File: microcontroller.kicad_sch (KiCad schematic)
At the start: 19 parts, among them J7 Conn_02x10_Odd_Even, J8 Conn_ST_STDC14, Q8 NPN, SW1 SW_Push, U10 MCP9808T-E/MS, U2 STM32G491KEU6

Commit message: PCB 2025 rev2
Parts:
- added R29, R30: 2k2, Resistor_SMD:R_0805_2012Metric_Pad1.20x1.40mm_HandSolder, symbol Device:R
- added TP10, TP9: TestPoint, TestPoint:TestPoint_Bridge_Pitch2.0mm_Drill0.7mm, symbol Connector:TestPoint
- C11: value 4.7u -> 4u7
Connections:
- net 3V3: now also R29.2, R30.1
- net SCL: now also R29.1, TP9.1
- net SDA: now also R30.2, TP10.1

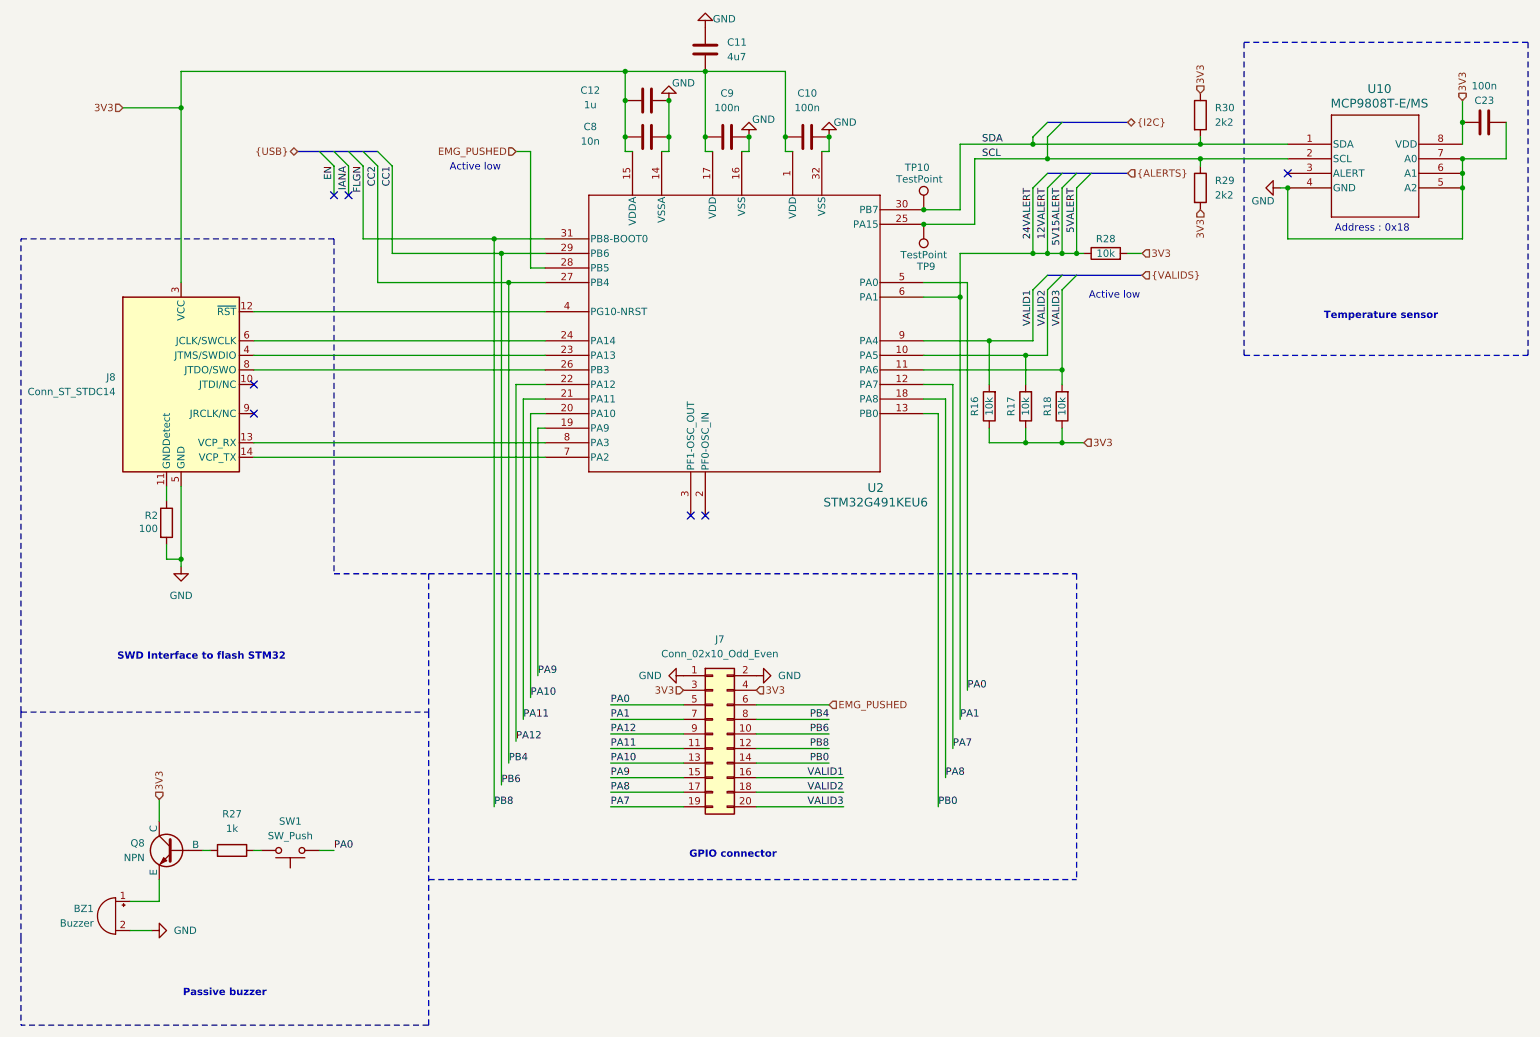
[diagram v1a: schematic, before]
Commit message: nouvelle version : correction erreurs, ameliorations qualite, passage a 4 couches, ajout pilotage des traco depuis le stm32
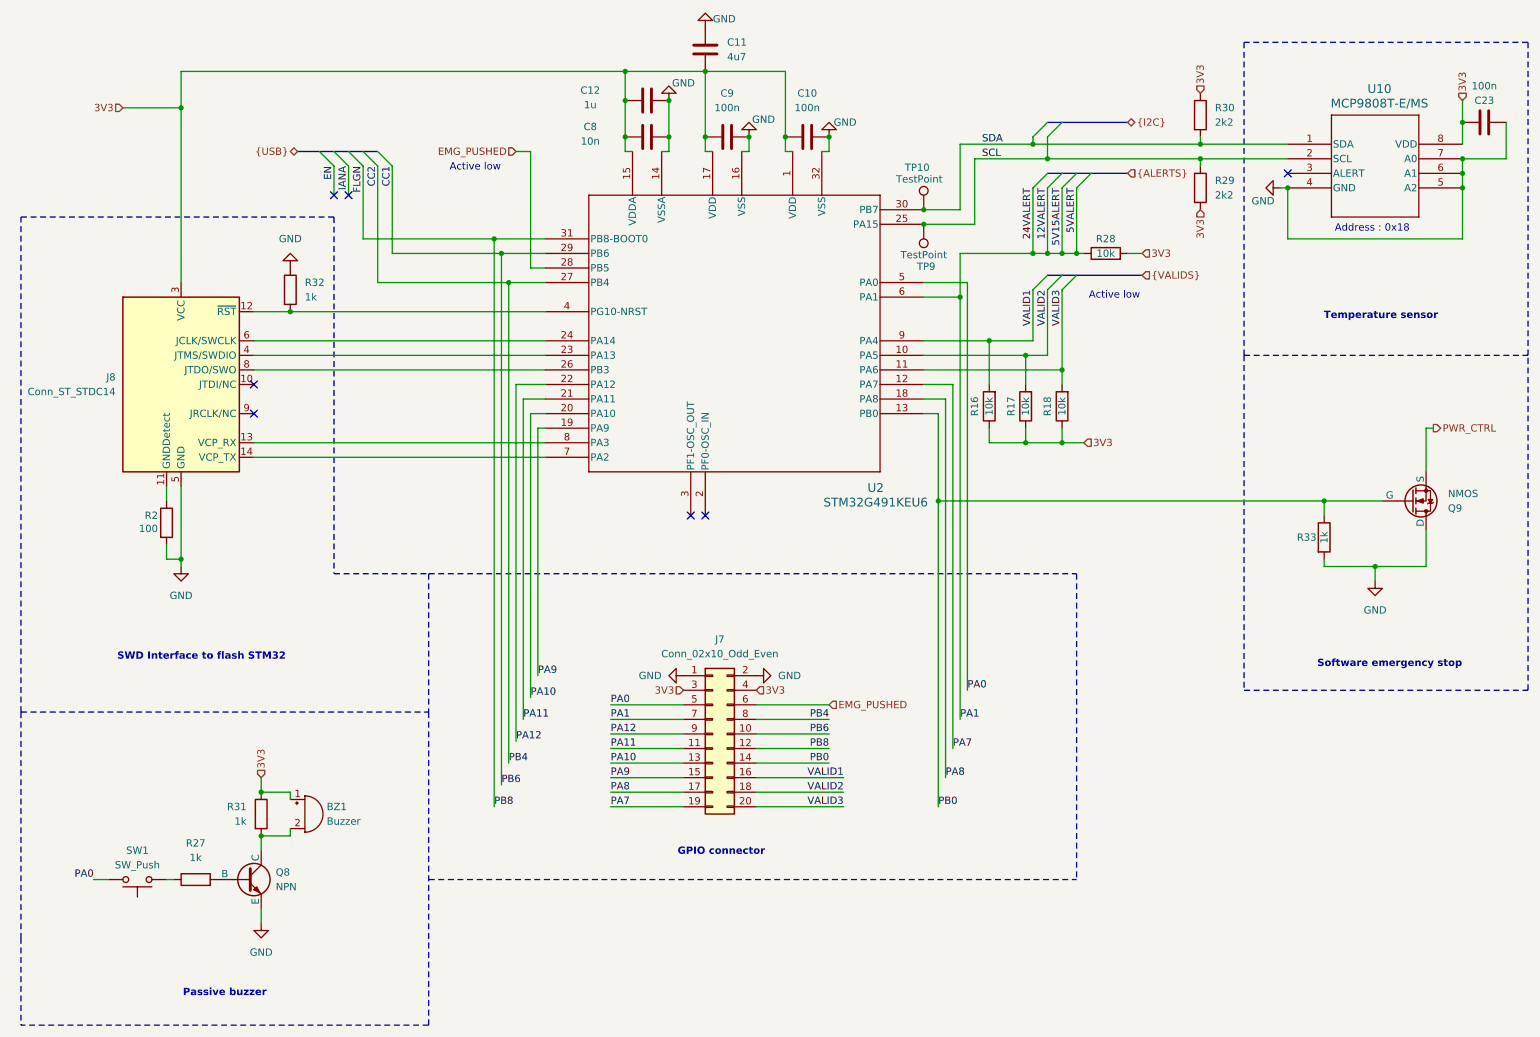
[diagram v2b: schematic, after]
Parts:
- added Q9: NMOS, Package_TO_SOT_SMD:SOT-23, symbol Simulation_SPICE:NMOS
- added R31, R32, R33: 1k, Resistor_SMD:R_0805_2012Metric_Pad1.20x1.40mm_HandSolder, symbol Device:R
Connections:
- net 3V3: now also BZ1.1 (+), R31.1; no longer Q8.1 (C)
- net GND: now also Q8.1 (E), Q9.3 (D), R32.1, R33.2; no longer BZ1.2 (-)
- net PB0: now also Q9.2 (G), R33.1
- net at Q8.3 (C): now also BZ1.2 (-), R31.2; no longer BZ1.1 (+)
- net at J8.12 (~{RST}), U2.4 (PG10-NRST): now also R32.2
- new net PWR_CTRL: Q9.1 (S)
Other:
- note added: "Software emergency stop"
- moved on the sheet: BZ1, Q8
